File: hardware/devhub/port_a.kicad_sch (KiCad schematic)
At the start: 16 parts, among them J1 USB-A, Q1 AO3400A, SW1 porta on/off, U1 TS3USB30E

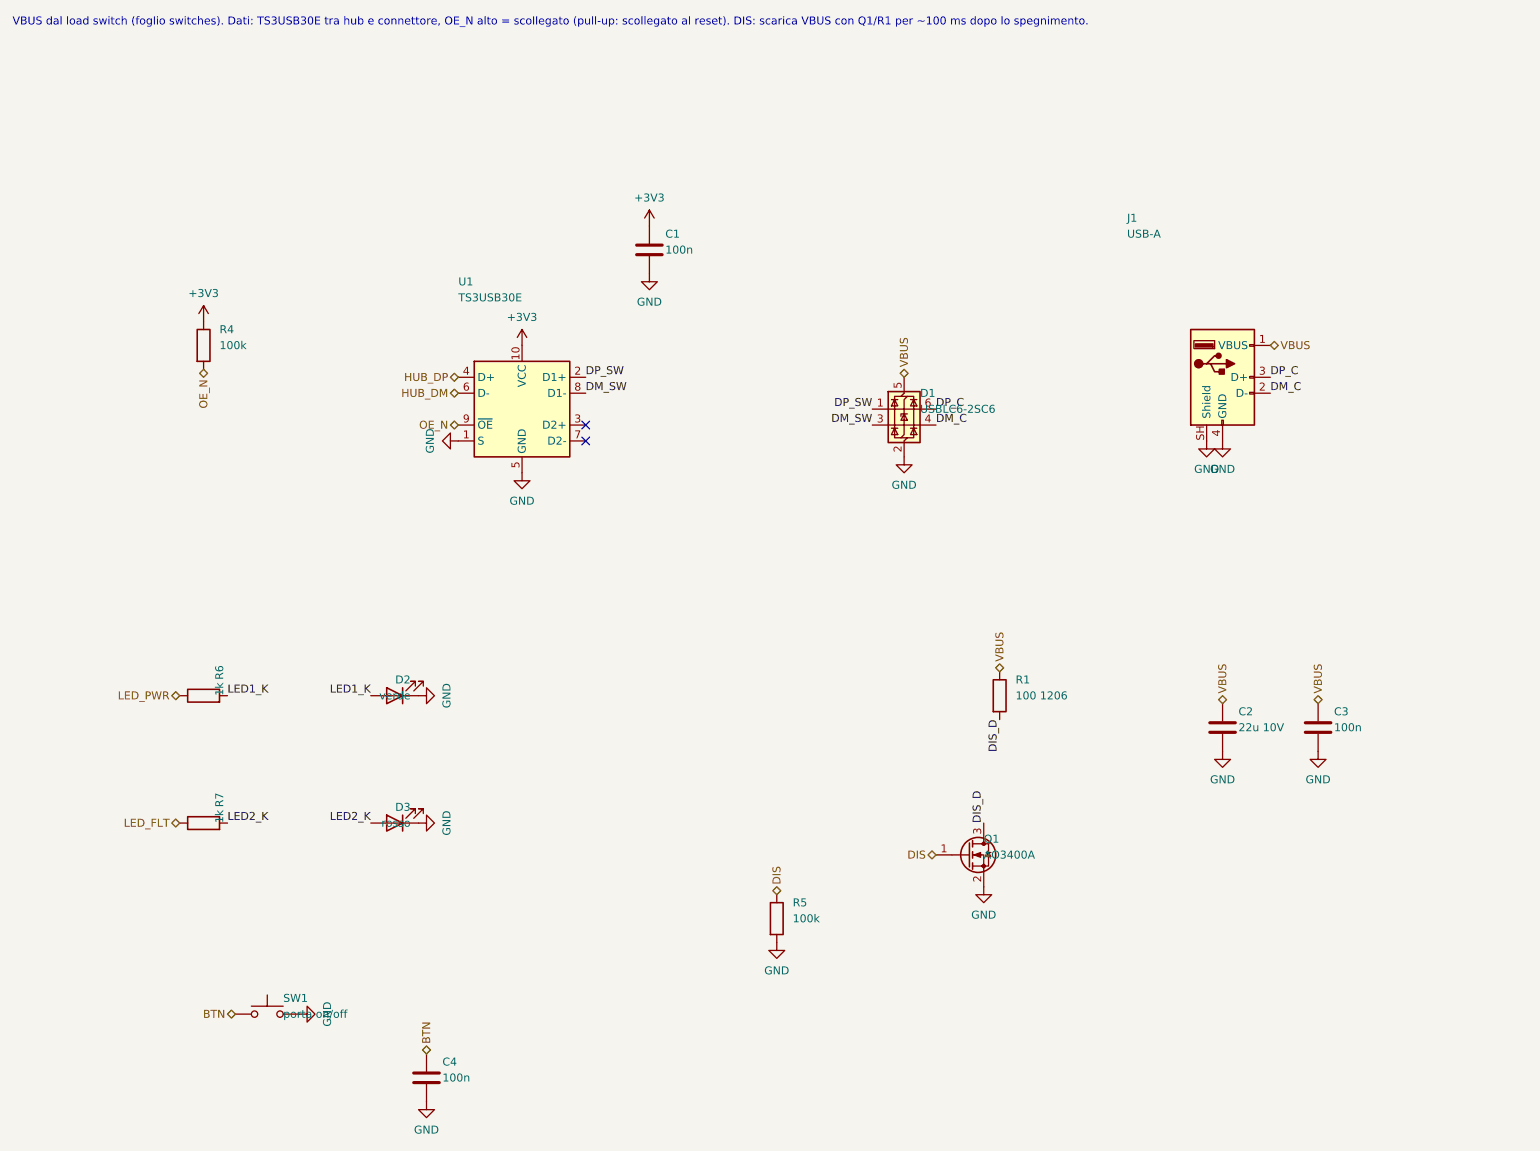
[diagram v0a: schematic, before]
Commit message: Schematic v0.2: hub reset supervisor, 1 A LDO, reorganized sheets, USB connectors and crystal
Functional changes:
- USB2517 RESET_N with pull-up and MCP120T-300 supervisor, wired-OR with
  the MCU (open-drain): resetting the MCU no longer resets the hub, so the
  ST DFU bootloader is reachable through it (D16/D17).
- 3.3 V LDO: AP7361C-33E (1 A, SOT-223) instead of AP2112K, which
  dissipated too much with the hub load.
- 74HC595 /OE on PB6 with pull-up: LEDs off until firmware enables them.
- Orange D93 instead of blue, USB-A bulk capacitance >= 120 uF, relay coil
  pinout fixed, snubbers marked DNP, Cliff FCR7350 banana jack footprints.
- D18: horizontal USB connectors, GCT USB4105-GF-A (USB-C) and Kycon
  KUSBX-AS1N-B (USB-A).
- D19: YXC X322524MOB4SI 24 MHz crystal (C_L 12 pF), 15 pF C0G load caps.

Layout: nearby parts wired directly, every net still explicitly named;
local labels inside sheets, global only across sheets, hierarchical for
ports. Files saved with KiCad 10.

Connectivity checked against the previous netlist, ERC clean.
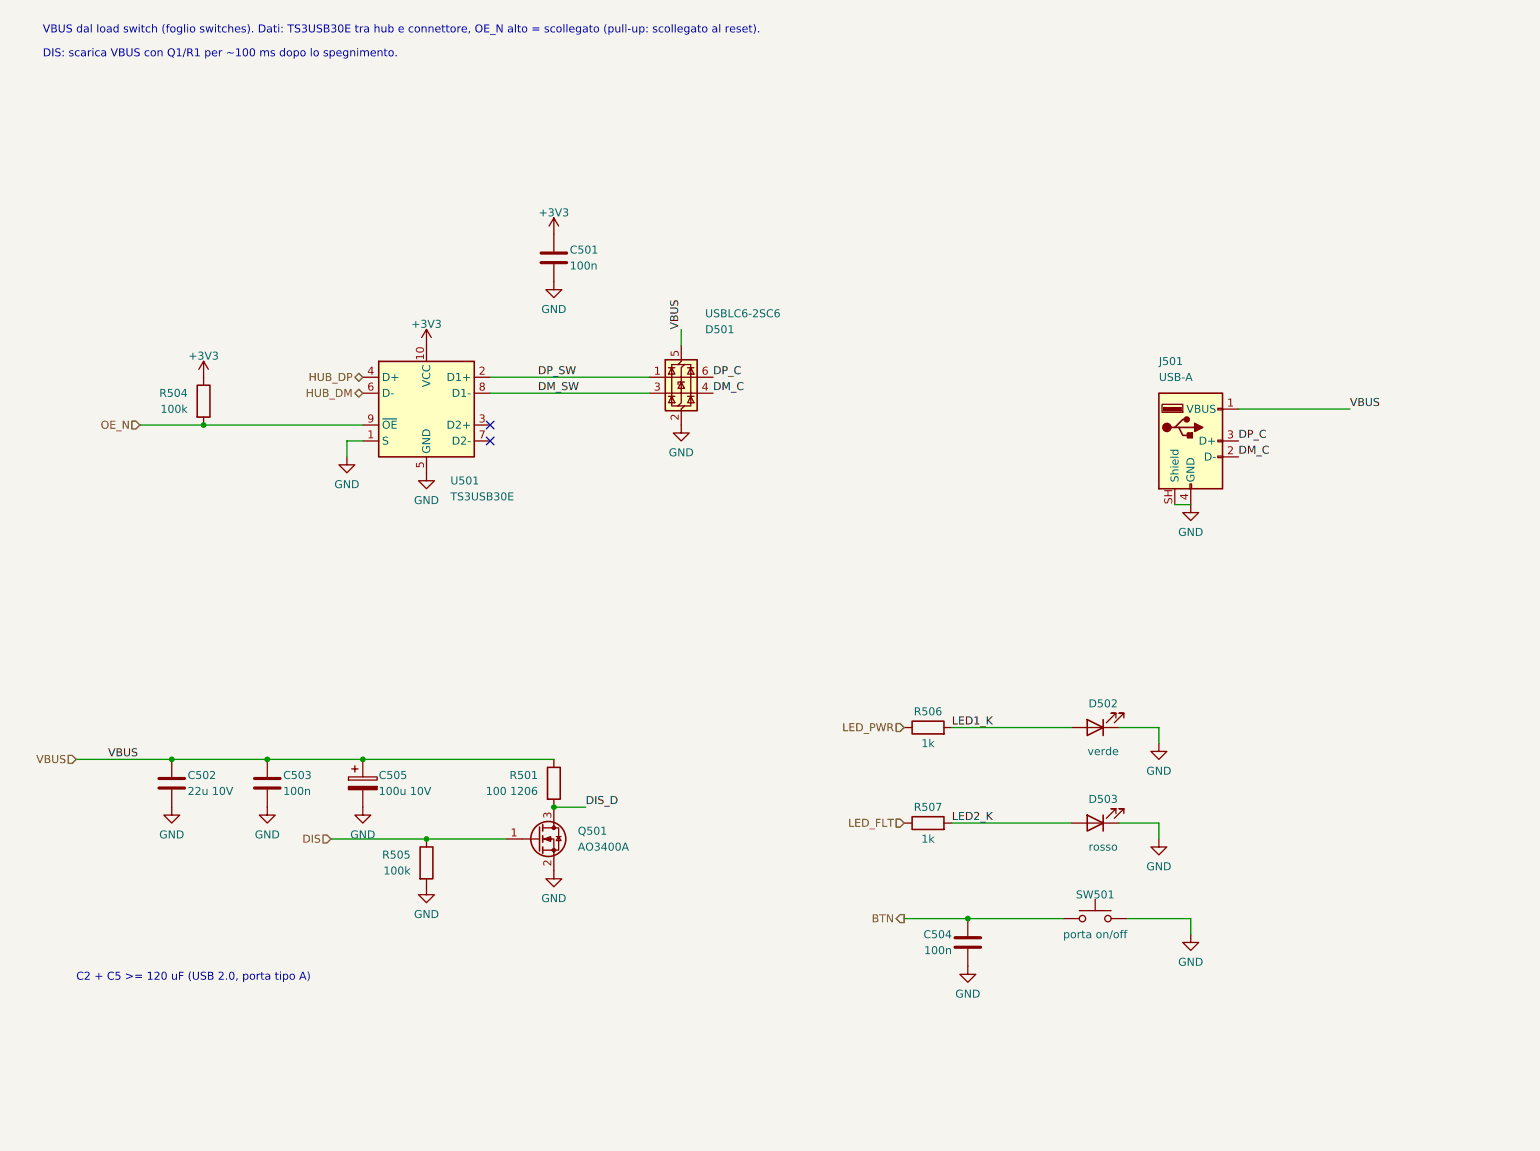
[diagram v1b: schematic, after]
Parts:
- removed C1, C3, C4: 100n, Capacitor_SMD:C_0603_1608Metric, symbol Device:C
- removed C2: 22u 10V, Capacitor_SMD:C_0805_2012Metric, symbol Device:C
- removed D1: USBLC6-2SC6, Package_TO_SOT_SMD:SOT-23-6, symbol Power_Protection:USBLC6-2SC6
- removed D2: verde, LED_SMD:LED_0805_2012Metric, symbol Device:LED
- removed D3: rosso, LED_SMD:LED_0805_2012Metric, symbol Device:LED
- removed J1: USB-A, Connector_USB:USB_A_Kycon_KUSBX-AS1N-B_Horizontal, symbol Connector:USB_A
- removed Q1: AO3400A, Package_TO_SOT_SMD:SOT-23, symbol Transistor_FET:AO3400A
- removed R1: 100 1206, Resistor_SMD:R_1206_3216Metric, symbol Device:R
- removed R4, R5: 100k, Resistor_SMD:R_0603_1608Metric, symbol Device:R
- removed R6, R7: 1k, Resistor_SMD:R_0603_1608Metric, symbol Device:R
- removed SW1: porta on/off, Button_Switch_THT:SW_PUSH_6mm_H13mm, symbol Switch:SW_Push
- removed U1: TS3USB30E, Package_SO:TSSOP-10_3x3mm_P0.5mm, symbol Interface_USB:TS3USB30EDGSR
- added C501, C503, C504: 100n, Capacitor_SMD:C_0603_1608Metric, symbol Device:C
- added C502: 22u 10V, Capacitor_SMD:C_0805_2012Metric, symbol Device:C
- added C505: 100u 10V, Capacitor_SMD:CP_Elec_6.3x7.7, symbol Device:C_Polarized
- added D501: USBLC6-2SC6, Package_TO_SOT_SMD:SOT-23-6, symbol Power_Protection:USBLC6-2SC6
- added D502: verde, LED_SMD:LED_0805_2012Metric, symbol Device:LED
- added D503: rosso, LED_SMD:LED_0805_2012Metric, symbol Device:LED
- added J501: USB-A, Connector_USB:USB_A_Kycon_KUSBX-AS1N-B_Horizontal, symbol Connector:USB_A
- added Q501: AO3400A, Package_TO_SOT_SMD:SOT-23, symbol Transistor_FET:AO3400A
- added R501: 100 1206, Resistor_SMD:R_1206_3216Metric, symbol Device:R
- added R504, R505: 100k, Resistor_SMD:R_0603_1608Metric, symbol Device:R
- added R506, R507: 1k, Resistor_SMD:R_0603_1608Metric, symbol Device:R
- added SW501: porta on/off, Button_Switch_THT:SW_PUSH_6mm_H13mm, symbol Switch:SW_Push
- added U501: TS3USB30E, Package_SO:TSSOP-10_3x3mm_P0.5mm, symbol Interface_USB:TS3USB30EDGSR
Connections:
- net +3V3: now also C501.1, R504.1, U501.10 (VCC)
- net BTN: now also C504.1, SW501.1
- net DIS: now also Q501.1 (G), R505.1
- net DIS_D: now also Q501.3 (D), R501.2
- net DM_C: now also D501.4 (I/O2), J501.2 (D-)
- net DM_SW: now also D501.3 (I/O2), U501.8 (D1-)
- net DP_C: now also D501.6 (I/O1), J501.3 (D+)
- net DP_SW: now also D501.1 (I/O1), U501.2 (D1+)
- net GND: now also C501.2, C502.2, C503.2, C504.2, C505.2, D501.2 (GND), D502.1 (K), D503.1 (K), J501.4 (GND), J501.SH (Shield), Q501.2 (S), R505.2, SW501.2, U501.1 (S), U501.5 (GND)
- net HUB_DM: now also U501.6 (D-)
- net HUB_DP: now also U501.4 (D+)
- net LED1_K: now also D502.2 (A), R506.2
- net LED2_K: now also D503.2 (A), R507.2
- net LED_FLT: now also R507.1
- net LED_PWR: now also R506.1
- net OE_N: now also R504.2, U501.9 (~{OE})
- net VBUS: now also C502.1, C503.1, C505.1, D501.5 (VBUS), J501.1 (VBUS), R501.1
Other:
- note added: "C2 + C5 >= 120 uF (USB 2.0, porta tipo A)"
- note added: "DIS: scarica VBUS con Q1/R1 per ~100 ms dopo lo spegnimento."
- note added: "VBUS dal load switch (foglio switches). Dati: TS3USB30E tra hub e connettore, OE_N alto = scollegato (pull-up: scollegato al reset)."
- note removed: "VBUS dal load switch (foglio switches). Dati: TS3USB30E tra hub e connettore, OE_N alto = scollegato (pull-up: scollegato al reset). DIS: scarica VBUS con Q1/R1 per ~100 ms dopo lo spegnimento."

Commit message: Lab-use protection: TPS259470A input eFuse, PI3USB4002A data switches; AGENTS.md
Power input (D20, D21):
- TPS259470A eFuse after the shunt: trips above 5.84 V and below 4.0 V,
  zener on EN to withstand up to 28 V, 3.5 A limit, ~5 ms soft start,
  auto-retry, FLT to the MCU on PB1.
- The shunt stays before the eFuse, so the INA3221 still measures the input
  voltage when the eFuse is off.

Ports (D22): PI3USB4002A instead of TS3USB30E. The connector side withstands
24 V and opens above 4.75 V, so a D+/D- short to VBUS on a board under test
no longer reaches the 3.3 V rail.

Symbols for both ICs added to the project library. AGENTS.md added: the
schematic is edited in KiCad or with targeted changes, never regenerated by
script. Sheets re-saved by KiCad.

Connectivity checked against the previous netlist, ERC clean.
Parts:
- added C506: 1u 25V, Capacitor_SMD:C_0805_2012Metric, symbol Device:C
- U501: value TS3USB30E -> PI3USB4002A; footprint Package_SO:TSSOP-10_3x3mm_P0.5mm -> (none); symbol Interface_USB:TS3USB30EDGSR -> devhub:PI3USB4002A
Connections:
- net DM_SW: now also U501.7 (C0-); no longer U501.8 (D1-)
- net DP_SW: now also U501.8 (C0+); no longer U501.2 (D1+)
- net GND: now also C506.2; no longer U501.1 (S)
- net HUB_DM: now also U501.2 (L0-); no longer U501.6 (D-)
- net HUB_DP: now also U501.1 (L0+); no longer U501.4 (D+)
- new net SW_REF: C506.1, U501.6 (REF)
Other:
- note added: "VBUS dal load switch (foglio switches). Dati: PI3USB4002A tra hub e connettore, OE_N (EN) alto = scollegato (pull-up: scollegato al reset); lato connettore tollera 24 V e si apre da solo sopra 4,75 V."
- note removed: "VBUS dal load switch (foglio switches). Dati: TS3USB30E tra hub e connettore, OE_N alto = scollegato (pull-up: scollegato al reset)."
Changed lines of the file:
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@@
 	(text "DIS: scarica VBUS con Q1/R1 per ~100 ms dopo lo spegnimento."
 		(exclude_from_sim no)
-		(at 14.986 20.32 0)
+		(at 10.16 20.32 0)
 		(effects
 			(font
@@
 		)
 	)
-	(text "VBUS dal load switch (foglio switches). Dati: TS3USB30E tra hub e connettore, OE_N alto = scollegato (pull-up: scollegato al reset)."
-		(exclude_from_sim no)
-		(at 14.986 16.51 0)
+	(text "VBUS dal load switch (foglio switches). Dati: PI3USB4002A tra hub e connettore, OE_N (EN) alto = scollegato (pull-up: scollegato al reset); lato connettore tollera 24 V e si apre da solo sopra 4,75 V."
+		(exclude_from_sim no)
+		(at 10.16 16.51 0)
 		(effects
 			(font
@@
 	)
 	(no_connect
-		(at 86.36 78.74)
+		(at 66.04 81.28)
 	)
 	(wire
@@
 	(wire
 		(pts
-			(xy 193.04 142.24) (xy 193.04 144.78)
+			(xy 86.36 78.74) (xy 96.52 78.74)
 		)
 		(stroke
@@
 	(wire
 		(pts
-			(xy 193.04 127) (xy 193.04 129.54)
+			(xy 193.04 142.24) (xy 193.04 144.78)
 		)
 		(stroke
@@
 	(wire
 		(pts
-			(xy 35.56 132.08) (xy 50.8 132.08)
+			(xy 193.04 127) (xy 193.04 129.54)
 		)
 		(stroke
@@
 	(wire
 		(pts
-			(xy 66.04 81.28) (xy 63.5 81.28)
+			(xy 35.56 132.08) (xy 50.8 132.08)
 		)
 		(stroke
@@
 		(pts
 			(xy 86.36 73.66) (xy 111.76 73.66)
-		)
-		(stroke
-			(width 0)
-			(type default)
-		)
-	)
-	(wire
-		(pts
-			(xy 63.5 81.28) (xy 63.5 83.82)
 		)
 		(stroke
@@
 	(label "DM_C"
 		(at 205.74 83.82 0)
+		(effects
+			(font
+				(size 1.27 1.27)
+			)
+			(justify left bottom)
+		)
+	)
+	(label "SW_REF"
+		(at 87.63 78.74 0)
 		(effects
 			(font
@@
 	)
 	(symbol
+		(lib_id "power:GND")
+		(at 96.52 86.36 0)
+		(unit 1)
+		(body_style 1)
+		(exclude_from_sim no)
+		(in_bom yes)
+		(on_board yes)
+		(in_pos_files yes)
+		(dnp no)
+		(property "Reference" "#PWR5005"
+			(at 96.52 86.36 0)
+			(hide yes)
+			(show_name no)
+			(do_not_autoplace no)
+			(effects
+				(font
+					(size 1.27 1.27)
+				)
+			)
+		)
+		(property "Value" "GND"
+			(at 96.52 90.76 0)
+			(show_name no)
+			(do_not_autoplace no)
+			(effects
+				(font
+					(size 1.27 1.27)
+				)
+			)
+		)
+		(property "Footprint" ""
+			(at 96.52 86.36 0)
+			(hide yes)
+			(show_name no)
+			(do_not_autoplace no)
+			(effects
+				(font
+					(size 1.27 1.27)
+				)
+			)
+		)
+		(property "Datasheet" ""
+			(at 96.52 86.36 0)
+			(hide yes)
+			(show_name no)
+			(do_not_autoplace no)
+			(effects
+				(font
+					(size 1.27 1.27)
+				)
+			)
+		)
+		(property "Description" ""
+			(at 96.52 86.36 0)
+			(hide yes)
+			(show_name no)
+			(do_not_autoplace no)
+			(effects
+				(font
+					(size 1.27 1.27)
+				)
+			)
+		)
+		(pin "1"
+		)
+		(instances
+			(project "devhub"
+				(path "/af6ea7d8-d1ba-5fc6-aec8-abf514847630/0c5617cc-af51-5b03-9838-7bc06ac23dd1"
+					(reference "#PWR5005")
+					(unit 1)
+				)
+			)
+		)
+	)
+	(symbol
 		(lib_id "Device:R")
 		(at 156.21 127 90)
@@
 	)
 	(symbol
-		(lib_id "Interface_USB:TS3USB30EDGSR")
+		(lib_id "devhub:PI3USB4002A")
 		(at 76.2 76.2 0)
 		(unit 1)
@@
 			)
 		)
-		(property "Value" "TS3USB30E"
+		(property "Value" "PI3USB4002A"
 			(at 80.01 90.17 0)
 			(show_name no)
@@
 			)
 		)
-		(property "Footprint" "Package_SO:TSSOP-10_3x3mm_P0.5mm"
+		(property "Footprint" ""
 			(at 76.2 76.2 0)
 			(hide yes)
@@
 			)
 		)
-		(property "Datasheet" "https://www.ti.com/lit/ds/symlink/ts3usb30e.pdf"
+		(property "Datasheet" "https://www.diodes.com/part/view/PI3USB4002A"
 			(at 76.2 76.2 0)
 			(hide yes)
@@
 			)
 		)
-		(property "Description" "ESD-Protected, High-Speed USB 2.0 (480-Mbps) 1:2 Multiplexer/Demultiplexer Switch With Single Enable, TSSOP-10 (Texas DGS0010A / VSSOP)"
+		(property "Description" "USB 2.0 SPST switch with 24 V tolerant port side and 4.75 V OVP, UQFN-10 1.5x2 mm (ZUA)"
 			(at 76.2 76.2 0)
 			(hide yes)
@@
 		(pin "2"
 		)
+		(pin "9"
+		)
 		(pin "3"
 		)
+		(pin "8"
+		)
+		(pin "7"
+		)
+		(pin "6"
+		)
 		(pin "4"
 		)
+		(pin "10"
+		)
 		(pin "5"
-		)
-		(pin "6"
-		)
-		(pin "7"
-		)
-		(pin "8"
-		)
-		(pin "9"
-		)
-		(pin "10"
 		)
 		(instances
@@
 		(in_pos_files yes)
 		(dnp no)
-		(property "Reference" "#PWR5002"
+		(property "Reference" "#PWR5001"
 			(at 76.2 66.04 0)
 			(hide yes)
@@
 			(project "devhub"
 				(path "/af6ea7d8-d1ba-5fc6-aec8-abf514847630/0c5617cc-af51-5b03-9838-7bc06ac23dd1"
-					(reference "#PWR5002")
+					(reference "#PWR5001")
 					(unit 1)
 				)
@@
 		(in_pos_files yes)
 		(dnp no)
-		(property "Reference" "#PWR5001"
+		(property "Reference" "#PWR5002"
 			(at 76.2 86.36 0)
 			(hide yes)
@@
 			(project "devhub"
 				(path "/af6ea7d8-d1ba-5fc6-aec8-abf514847630/0c5617cc-af51-5b03-9838-7bc06ac23dd1"
-					(reference "#PWR5001")
+					(reference "#PWR5002")
 					(unit 1)
 				)
@@
 	)
 	(symbol
-		(lib_id "power:GND")
-		(at 63.5 83.82 0)
-		(unit 1)
-		(body_style 1)
-		(exclude_from_sim no)
-		(in_bom yes)
-		(on_board yes)
-		(in_pos_files yes)
-		(dnp no)
-		(property "Reference" "#PWR5005"
-			(at 63.5 83.82 0)
-			(hide yes)
-			(show_name no)
-			(do_not_autoplace no)
-			(effects
-				(font
-					(size 1.27 1.27)
-				)
-			)
-		)
-		(property "Value" "GND"
-			(at 63.5 88.22 0)
-			(show_name no)
-			(do_not_autoplace no)
-			(effects
-				(font
-					(size 1.27 1.27)
-				)
-			)
-		)
-		(property "Footprint" ""
-			(at 63.5 83.82 0)
-			(hide yes)
-			(show_name no)
-			(do_not_autoplace no)
-			(effects
-				(font
-					(size 1.27 1.27)
-				)
-			)
-		)
-		(property "Datasheet" ""
-			(at 63.5 83.82 0)
-			(hide yes)
-			(show_name no)
-			(do_not_autoplace no)
-			(effects
-				(font
-					(size 1.27 1.27)
-				)
-			)
-		)
-		(property "Description" ""
-			(at 63.5 83.82 0)
-			(hide yes)
-			(show_name no)
-			(do_not_autoplace no)
-			(effects
-				(font
-					(size 1.27 1.27)
-				)
-			)
-		)
-		(pin "1"
-		)
-		(instances
-			(project "devhub"
-				(path "/af6ea7d8-d1ba-5fc6-aec8-abf514847630/0c5617cc-af51-5b03-9838-7bc06ac23dd1"
-					(reference "#PWR5005")
-					(unit 1)
-				)
-			)
-		)
-	)
-	(symbol
 		(lib_id "Power_Protection:USBLC6-2SC6")
 		(at 116.84 71.12 0)
@@
 					(unit 1)
 				)
+			)
+		)
+	)
+	(symbol
+		(lib_id "Device:C")
+		(at 96.52 82.55 0)
+		(unit 1)
+		(body_style 1)
+		(exclude_from_sim no)
+		(in_bom yes)
+		(on_board yes)
+		(in_pos_files yes)
+		(dnp no)
+		(property "Reference" "C506"
+			(at 99.06 81.28 0)
+			(show_name no)
+			(do_not_autoplace no)
+			(effects
+				(font
+					(size 1.27 1.27)
+				)
+				(justify left)
+			)
+		)
+		(property "Value" "1u 25V"
+			(at 99.06 83.82 0)
+			(show_name no)
+			(do_not_autoplace no)
+			(effects
+				(font
+					(size 1.27 1.27)
+				)
+				(justify left)
+			)
+		)
+		(property "Footprint" "Capacitor_SMD:C_0805_2012Metric"
+			(at 96.52 82.55 0)
+			(hide yes)
+			(show_name no)
+			(do_not_autoplace no)
+			(effects
+				(font
+					(size 1.27 1.27)
+				)
+			)
+		)
+		(property "Datasheet" ""
+			(at 96.52 82.55 0)
+			(hide yes)
+			(show_name no)
+			(do_not_autoplace no)
+			(effects
+				(font
+					(size 1.27 1.27)
+				)
+			)
+		)
+		(property "Description" "Unpolarized capacitor"
+			(at 96.52 82.55 0)
+			(hide yes)
+			(show_name no)
+			(do_not_autoplace no)
+			(effects
+				(font
+					(size 1.27 1.27)
+				)
+			)
+		)
+		(pin "1"
+		)
+		(pin "2"
+		)
+		(instances
+			(project "devhub"
+				(path "/af6ea7d8-d1ba-5fc6-aec8-abf514847630/0c5617cc-af51-5b03-9838-7bc06ac23dd1"
+					(reference "C506")
+					(unit 1)
+				)
